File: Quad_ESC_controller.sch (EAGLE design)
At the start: 23 parts, among them Y1 ECS-80-S-4X

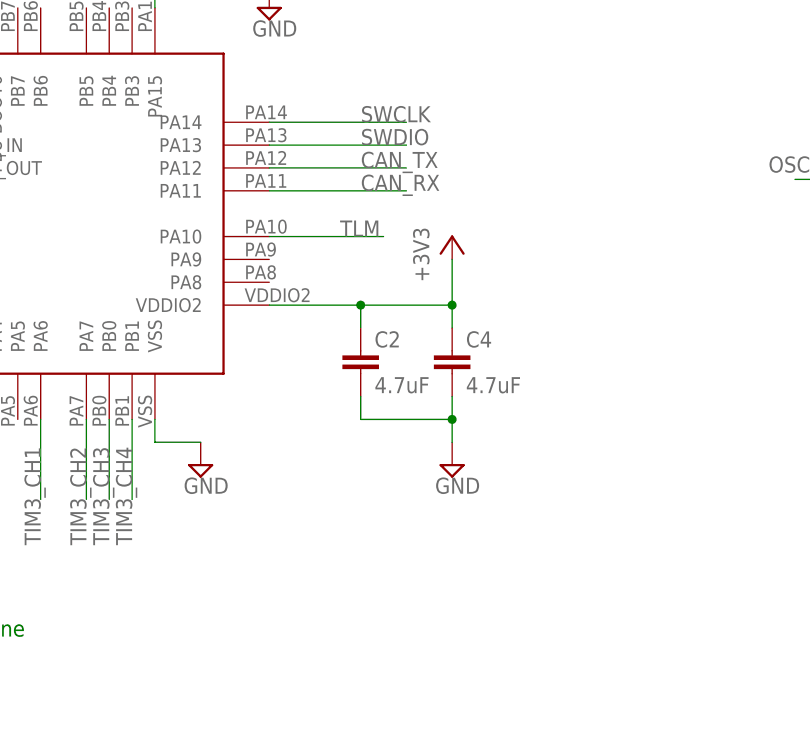
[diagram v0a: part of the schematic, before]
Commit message: Added 1k Resistor TLM -> 3.3V
also tried airwiring it lol. it's v bad, but that is next year's problem.
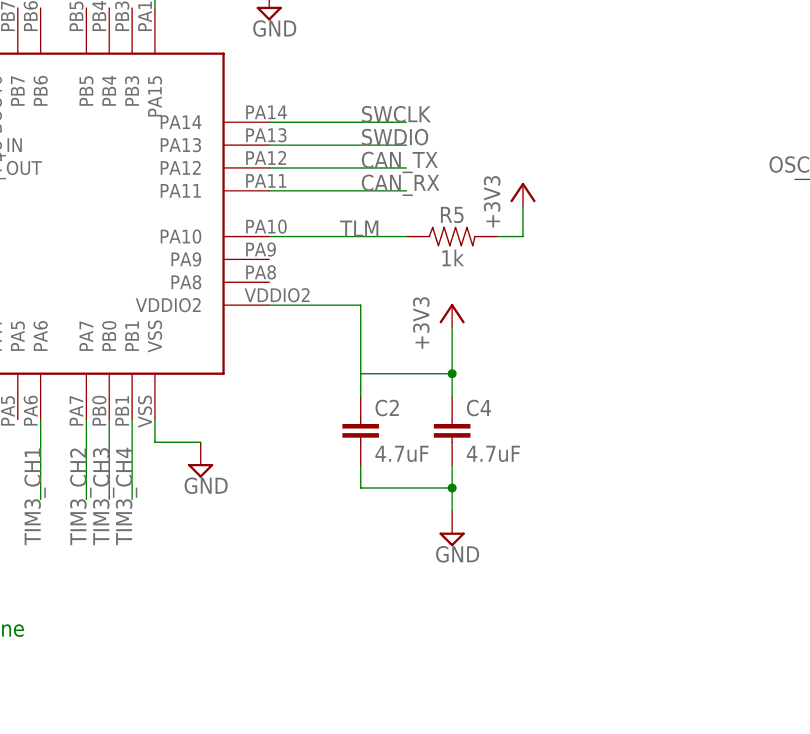
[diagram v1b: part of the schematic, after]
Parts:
- added R5: 1k, SparkFun-Resistors:RESISTOR0603
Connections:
- net +3V3: now also R5.2
- net TLM: now also R5.1
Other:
- moved on the sheet: C2, C4
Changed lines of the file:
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@@
 <part name="SUPPLY1" library="supply2" library_urn="urn:adsk.eagle:library:372" deviceset="GND" device=""/>
 <part name="+3V6" library="supply1" library_urn="urn:adsk.eagle:library:371" deviceset="+3V3" device=""/>
+<part name="R5" library="SparkFun-Resistors" library_urn="urn:adsk.eagle:library:532" deviceset="RESISTOR" device="0603" package3d_urn="urn:adsk.eagle:package:39650/1" value="1k"/>
+<part name="+3V7" library="supply1" library_urn="urn:adsk.eagle:library:371" deviceset="+3V3" device=""/>
 </parts>
 <sheets>
@@
 <attribute name="VALUE" x="32.004" y="148.971" size="1.778" layer="96" font="vector"/>
 </instance>
-<instance part="C2" gate="G$1" x="119.38" y="118.11" smashed="yes">
-<attribute name="NAME" x="120.904" y="121.031" size="1.778" layer="95" font="vector"/>
-<attribute name="VALUE" x="120.904" y="115.951" size="1.778" layer="96" font="vector"/>
+<instance part="C2" gate="G$1" x="119.38" y="110.49" smashed="yes">
+<attribute name="NAME" x="120.904" y="113.411" size="1.778" layer="95" font="vector"/>
+<attribute name="VALUE" x="120.904" y="108.331" size="1.778" layer="96" font="vector"/>
 </instance>
 <instance part="C3" gate="G$1" x="45.72" y="151.13" smashed="yes">
@@
 <attribute name="VALUE" x="47.244" y="148.971" size="1.778" layer="96" font="vector"/>
 </instance>
-<instance part="C4" gate="G$1" x="129.54" y="118.11" smashed="yes">
-<attribute name="NAME" x="131.064" y="121.031" size="1.778" layer="95" font="vector"/>
-<attribute name="VALUE" x="131.064" y="115.951" size="1.778" layer="96" font="vector"/>
+<instance part="C4" gate="G$1" x="129.54" y="110.49" smashed="yes">
+<attribute name="NAME" x="131.064" y="113.411" size="1.778" layer="95" font="vector"/>
+<attribute name="VALUE" x="131.064" y="108.331" size="1.778" layer="96" font="vector"/>
 </instance>
 <instance part="C5" gate="G$1" x="40.64" y="113.03" smashed="yes">
@@
 <attribute name="VALUE" x="107.315" y="155.575" size="1.778" layer="96"/>
 </instance>
-<instance part="GND7" gate="GND" x="129.54" y="107.95" smashed="yes">
-<attribute name="VALUE" x="127.635" y="104.775" size="1.778" layer="96"/>
-</instance>
-<instance part="+3V4" gate="G$1" x="129.54" y="133.35" smashed="yes">
-<attribute name="VALUE" x="127" y="128.27" size="1.778" layer="96" rot="R90"/>
+<instance part="GND7" gate="GND" x="129.54" y="100.33" smashed="yes">
+<attribute name="VALUE" x="127.635" y="97.155" size="1.778" layer="96"/>
+</instance>
+<instance part="+3V4" gate="G$1" x="129.54" y="125.73" smashed="yes">
+<attribute name="VALUE" x="127" y="120.65" size="1.778" layer="96" rot="R90"/>
 </instance>
 <instance part="+3V5" gate="G$1" x="40.64" y="128.27" smashed="yes">
@@
 <instance part="+3V6" gate="G$1" x="63.5" y="116.84" smashed="yes">
 <attribute name="VALUE" x="60.96" y="111.76" size="1.778" layer="96" rot="R90"/>
+</instance>
+<instance part="R5" gate="G$1" x="129.54" y="133.35" smashed="yes">
+<attribute name="NAME" x="129.54" y="134.874" size="1.778" layer="95" font="vector" align="bottom-center"/>
+<attribute name="VALUE" x="129.54" y="131.826" size="1.778" layer="96" font="vector" align="top-center"/>
+</instance>
+<instance part="+3V7" gate="G$1" x="137.414" y="139.192" smashed="yes">
+<attribute name="VALUE" x="134.874" y="134.112" size="1.778" layer="96" rot="R90"/>
 </instance>
 </instances>
@@
 <segment>
 <pinref part="C2" gate="G$1" pin="2"/>
-<wire x1="119.38" y1="115.57" x2="119.38" y2="113.03" width="0.1524" layer="91"/>
+<wire x1="119.38" y1="107.95" x2="119.38" y2="105.41" width="0.1524" layer="91"/>
 <pinref part="C4" gate="G$1" pin="2"/>
-<wire x1="119.38" y1="113.03" x2="129.54" y2="113.03" width="0.1524" layer="91"/>
-<wire x1="129.54" y1="113.03" x2="129.54" y2="115.57" width="0.1524" layer="91"/>
+<wire x1="119.38" y1="105.41" x2="129.54" y2="105.41" width="0.1524" layer="91"/>
+<wire x1="129.54" y1="105.41" x2="129.54" y2="107.95" width="0.1524" layer="91"/>
 <pinref part="GND7" gate="GND" pin="GND"/>
-<wire x1="129.54" y1="110.49" x2="129.54" y2="113.03" width="0.1524" layer="91"/>
-<junction x="129.54" y="113.03"/>
+<wire x1="129.54" y1="102.87" x2="129.54" y2="105.41" width="0.1524" layer="91"/>
+<junction x="129.54" y="105.41"/>
 </segment>
 <segment>
@@
 </segment>
 <segment>
+<pinref part="C2" gate="G$1" pin="1"/>
+<wire x1="119.38" y1="118.11" x2="119.38" y2="116.84" width="0.1524" layer="91"/>
+<pinref part="C4" gate="G$1" pin="1"/>
+<wire x1="119.38" y1="116.84" x2="119.38" y2="115.57" width="0.1524" layer="91"/>
+<wire x1="129.54" y1="115.57" x2="129.54" y2="118.11" width="0.1524" layer="91"/>
+<wire x1="129.54" y1="118.11" x2="119.38" y2="118.11" width="0.1524" layer="91"/>
+<pinref part="+3V4" gate="G$1" pin="+3V3"/>
+<wire x1="129.54" y1="118.11" x2="129.54" y2="123.19" width="0.1524" layer="91"/>
+<junction x="129.54" y="118.11"/>
 <pinref part="U$4" gate="G$1" pin="VDDIO2"/>
-<pinref part="C2" gate="G$1" pin="1"/>
 <wire x1="109.22" y1="125.73" x2="119.38" y2="125.73" width="0.1524" layer="91"/>
-<wire x1="119.38" y1="125.73" x2="119.38" y2="123.19" width="0.1524" layer="91"/>
-<pinref part="C4" gate="G$1" pin="1"/>
-<wire x1="129.54" y1="123.19" x2="129.54" y2="125.73" width="0.1524" layer="91"/>
-<wire x1="129.54" y1="125.73" x2="119.38" y2="125.73" width="0.1524" layer="91"/>
-<junction x="119.38" y="125.73"/>
-<pinref part="+3V4" gate="G$1" pin="+3V3"/>
-<wire x1="129.54" y1="125.73" x2="129.54" y2="130.81" width="0.1524" layer="91"/>
-<junction x="129.54" y="125.73"/>
+<wire x1="119.38" y1="125.73" x2="119.38" y2="118.11" width="0.1524" layer="91"/>
 </segment>
 <segment>
@@
 <pinref part="+3V6" gate="G$1" pin="+3V3"/>
 </segment>
+<segment>
+<pinref part="R5" gate="G$1" pin="2"/>
+<wire x1="134.62" y1="133.35" x2="137.414" y2="133.35" width="0.1524" layer="91"/>
+<wire x1="137.414" y1="133.35" x2="137.414" y2="136.652" width="0.1524" layer="91"/>
+<pinref part="+3V7" gate="G$1" pin="+3V3"/>
+</segment>
 </net>
 <net name="CAN_TX" class="0">
@@
 <segment>
 <pinref part="U$4" gate="G$1" pin="PA10"/>
-<wire x1="109.22" y1="133.35" x2="121.92" y2="133.35" width="0.1524" layer="91"/>
+<wire x1="109.22" y1="133.35" x2="124.46" y2="133.35" width="0.1524" layer="91"/>
 <label x="117.094" y="133.35" size="1.778" layer="95"/>
-</segment>
-</net>
+<pinref part="R5" gate="G$1" pin="1"/>
+</segment>
+</net>
